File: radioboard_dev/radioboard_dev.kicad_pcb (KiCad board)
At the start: 2 copper layers, 32.5 x 148.5 mm, 98 parts, among them J1 Conn_01x02, J2 Conn_01x02, J3 Conn_01x04, J4 Conn_01x04, J5 Conn_01x04, J6 Conn_01x04, J9 Conn_01x04, U1 TPS22917DBVR, U10 STM32WL55CCUx, U11 MAX17048G_T10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

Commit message: pre mass edit of footprints
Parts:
- C8: footprint parts:C0402 -> Capacitor_SMD:C_0402_1005Metric
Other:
- board size 32.5 x 148.5 mm -> 32.5 x 148.2 mm
- board text added: "Optional Clock"

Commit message: basically done
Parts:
- added G***: LOGO, LOGO, B.Cu at (43.0, 131.2)
- added REF**: MountingHole, parts:MountingHole, F.Cu at (25.2, 29.0)
- added REF**: MountingHole, parts:MountingHole, F.Cu at (51.2, 29.0)
- added REF**: MountingHole, parts:MountingHole, F.Cu at (25.2, 170.8)
- added REF**: MountingHole, parts:MountingHole, F.Cu at (51.2, 170.8)
- moved B1 9.82 mm to (26.8, 46.7), turned to 0 degrees
- moved LED1 2.24 mm to (50.5, 36.2)
- moved LED2 2.24 mm to (47.8, 36.2)
- moved R34 2.24 mm to (47.8, 39.0)
- moved R35 2.24 mm to (50.5, 39.0)
- moved J3 0.70 mm to (51.8, 74.1)
- renumbered LED2 to LED1, LED3 to LED2
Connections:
- U12 pad : (no net) -> GND
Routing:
- net +3.3V: track 4.30 -> 120.9 mm, vias 0 -> 5
- net GND: track 3.19 -> 87.1 mm, vias 0 -> 54
- net BUT1: track 34.6 -> 40.4 mm
- net LED1: track 17.2 -> 14.1 mm
- net LED2: track 14.6 -> 12.2 mm
- net Net-(U5-PROG): track 3.45 -> 1.75 mm
- net VDDRF1V55: track 26.4 -> 27.2 mm
- net VGPS: track 33.7 -> 34.4 mm
- net OSC_IN: track 12.4 -> 12.5 mm, vias 0 -> 2
- added copper zone on B.Cu, net GND
- added copper zone on F.Cu, net GND
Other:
- board text added: "+"
- board text added: "-"
- board text added: "B"
- board text added: "BUT1"
- board text added: "Dear RF Gods, Please let this work..."
- board text added: "Designed and built by"
- board text added: "Forrest Milner MBARI 7/10/2024"
- board text added: "GND RX TX 3V3"
- board text added: "GPS UART"
- board text added: "Kinéis Radio Board Engineer: Forrest Milner Mentor: Thom Maughan Summer 2024 MBARI"
- board text added: "RST"

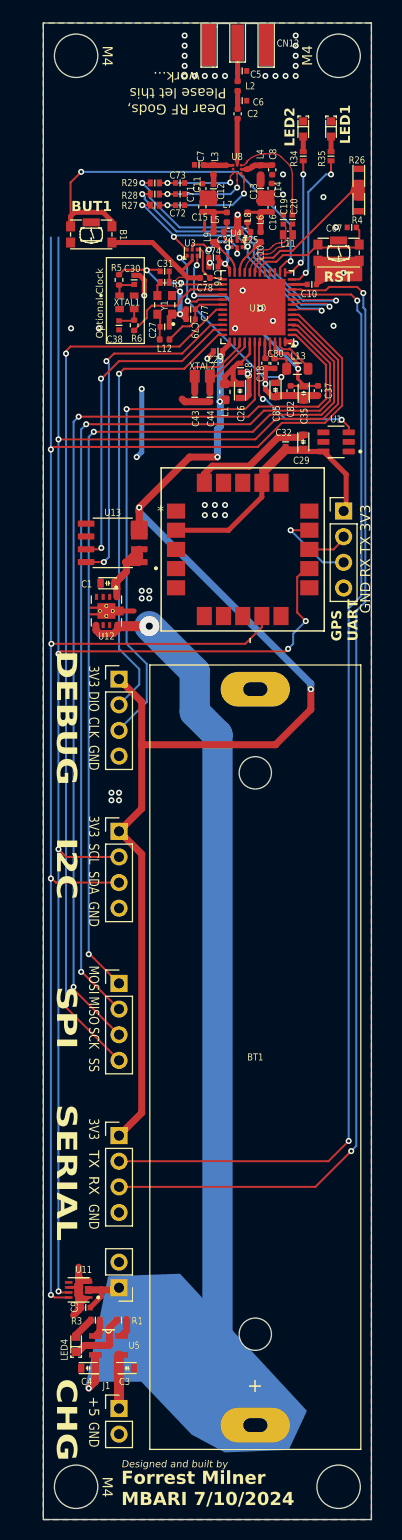
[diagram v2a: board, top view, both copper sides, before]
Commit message: DRC stitching
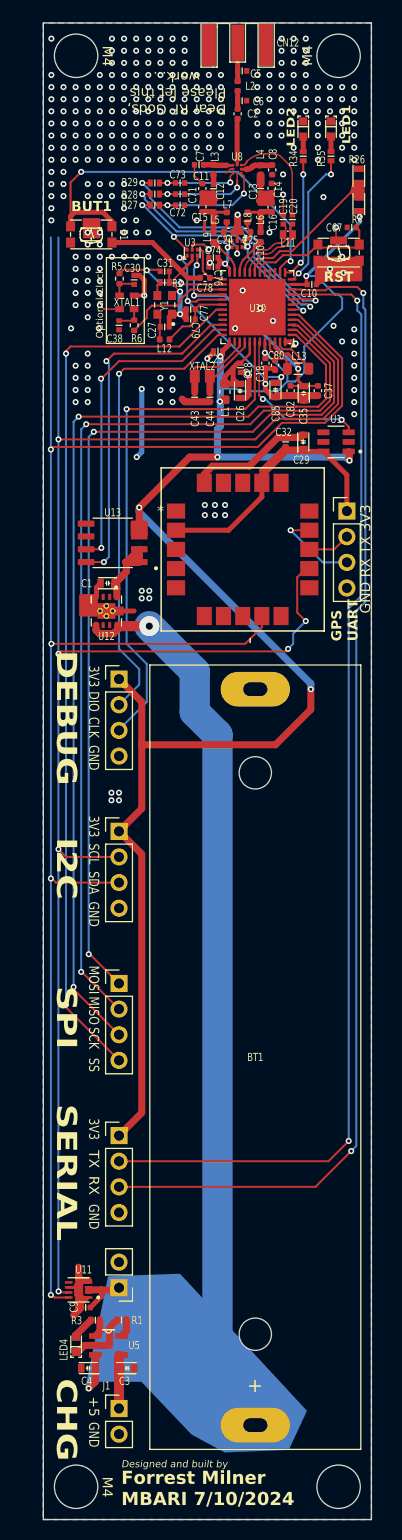
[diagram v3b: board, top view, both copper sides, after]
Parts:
- moved J3 0.32 mm to (52.1, 74.1)
- moved C80 0.19 mm to (45.0, 59.7)
- moved R5 0.13 mm to (29.5, 51.1)
- moved L13 0.08 mm to (47.2, 60.0)
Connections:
- U12 pad : GND -> (no net)
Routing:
- net +3.3V: track 120.9 -> 170.9 mm, vias 5 -> 9
- net GND: track 87.1 -> 98.2 mm, vias 54 -> 307
- net /microcontroller_RF/FE_CTRL2: track 29.6 -> 25.2 mm
- net /microcontroller_RF/FE_CTRL3: track 30.4 -> 26.4 mm
- net /microcontroller_RF/FE_CTRL1: track 29.2 -> 25.6 mm
- net Net-(U8-RF2): track 4.12 -> 6.06 mm
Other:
- board text added: "{ "ViaStitching": "0.2", "stich area": { "HSpacing": "1", "VSpacing": "1", "Clearance": "1", "Randomize": false } }"

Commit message: bom changes
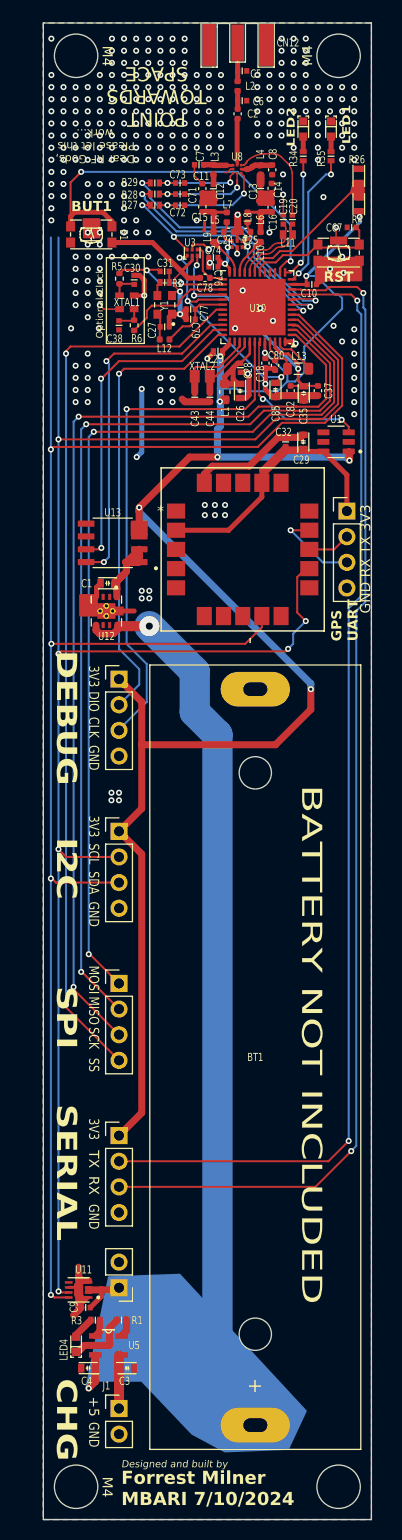
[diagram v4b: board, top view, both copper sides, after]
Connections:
- U12 pad : (no net) -> GND
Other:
- board text added: "BATTERY NOT INCLUDED"
- board text added: "POINT TOWARDS SPACE"

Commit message: datasgeers added...
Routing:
- added copper zone on In1.Cu, net GND
- added copper zone on In2.Cu, net GND
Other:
- copper layers 2 -> 4
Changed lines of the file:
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@@
 	(layers
 		(0 "F.Cu" signal)
+		(1 "In1.Cu" signal)
+		(2 "In2.Cu" signal)
 		(31 "B.Cu" signal)
 		(32 "B.Adhes" user "B.Adhesive")
@@
 	)
 	(setup
+		(stackup
+			(layer "F.SilkS"
+				(type "Top Silk Screen")
+			)
+			(layer "F.Paste"
+				(type "Top Solder Paste")
+			)
+			(layer "F.Mask"
+				(type "Top Solder Mask")
+				(thickness 0.01)
+			)
+			(layer "F.Cu"
+				(type "copper")
+				(thickness 0.035)
+			)
+			(layer "dielectric 1"
+				(type "prepreg")
+				(thickness 0.1)
+				(material "FR4")
+				(epsilon_r 4.5)
+				(loss_tangent 0.02)
+			)
+			(layer "In1.Cu"
+				(type "copper")
+				(thickness 0.035)
+			)
+			(layer "dielectric 2"
+				(type "core")
+				(thickness 1.24)
+				(material "FR4")
+				(epsilon_r 4.5)
+				(loss_tangent 0.02)
+			)
+			(layer "In2.Cu"
+				(type "copper")
+				(thickness 0.035)
+			)
+			(layer "dielectric 3"
+				(type "prepreg")
+				(thickness 0.1)
+				(material "FR4")
+				(epsilon_r 4.5)
+				(loss_tangent 0.02)
+			)
+			(layer "B.Cu"
+				(type "copper")
+				(thickness 0.035)
+			)
+			(layer "B.Mask"
+				(type "Bottom Solder Mask")
+				(thickness 0.01)
+			)
+			(layer "B.Paste"
+				(type "Bottom Solder Paste")
+			)
+			(layer "B.SilkS"
+				(type "Bottom Silk Screen")
+			)
+			(copper_finish "None")
+			(dielectric_constraints no)
+		)
 		(pad_to_mask_clearance 0)
 		(allow_soldermask_bridges_in_footprints no)
@@
 			(outputformat 1)
 			(mirror no)
-			(drillshape 1)
+			(drillshape 0)
 			(scaleselection 1)
-			(outputdirectory "")
+			(outputdirectory "fab/")
 		)
 	)
@@
 		(net 1)
 		(net_name "GND")
-		(layers "F&B.Cu")
+		(layers "F.Cu" "In1.Cu" "In2.Cu" "B.Cu")
 		(hatch edge 0.5)
 		(connect_pads
